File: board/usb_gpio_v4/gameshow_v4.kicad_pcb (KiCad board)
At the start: 2 copper layers, 160.8 x 51.3 mm, 27 parts, among them J1 NC3FAAH, J2 NC3FAAH, J3 NC3FAAH, J4 NC3FAAH

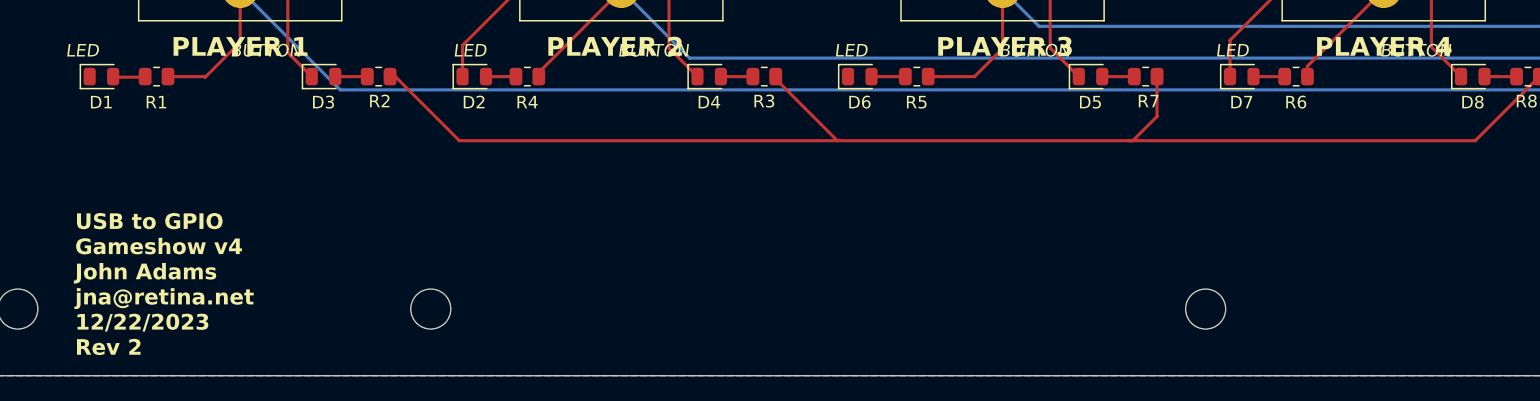
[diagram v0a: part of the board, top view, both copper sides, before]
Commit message: add test switches
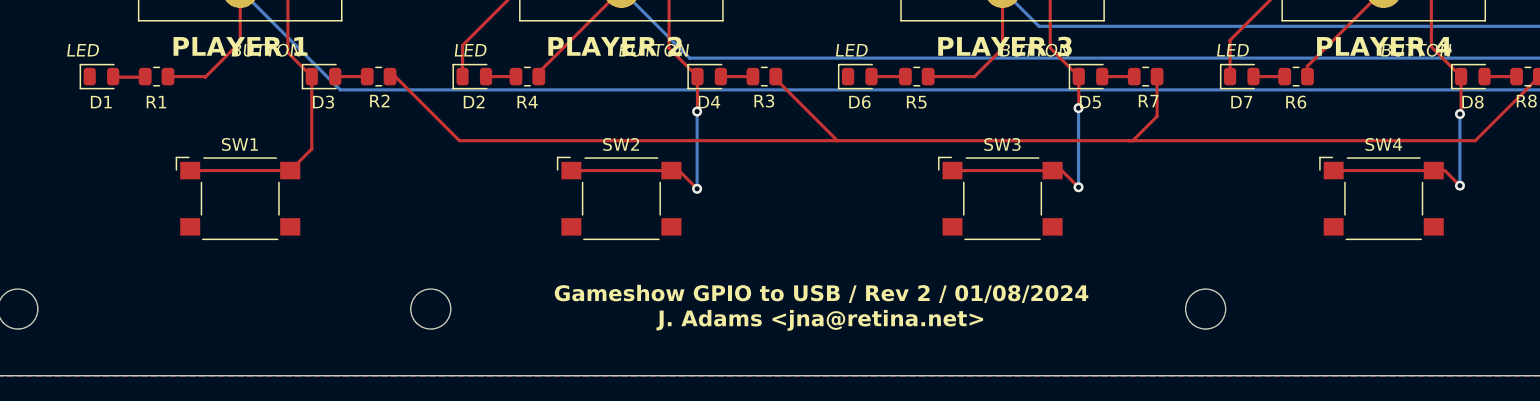
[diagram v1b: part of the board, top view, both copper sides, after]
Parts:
- added SW1: SW_SPST, Button_Switch_SMD:SW_SPST_Omron_B3FS-101xP, F.Cu at (92.7, 91.0)
- added SW2: SW_SPST, Button_Switch_SMD:SW_SPST_Omron_B3FS-101xP, F.Cu at (123.2, 91.0)
- added SW3: SW_SPST, Button_Switch_SMD:SW_SPST_Omron_B3FS-101xP, F.Cu at (153.7, 91.0)
- added SW4: SW_SPST, Button_Switch_SMD:SW_SPST_Omron_B3FS-101xP, F.Cu at (184.2, 91.0)
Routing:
- net P2_SW: track 106.9 -> 126.6 mm, vias 0 -> 2
- net P3_SW: track 75.4 -> 94.9 mm, vias 0 -> 2
- net P4_SW: track 44.3 -> 63.7 mm, vias 0 -> 2
- net P1_SW: track 122.0 -> 138.2 mm
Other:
- board text added: "Gameshow GPIO to USB / Rev 2 / 01/08/2024 J. Adams <jna@retina.net>"
- board text removed: "USB to GPIO Gameshow v4 John Adams jna@retina.net 12/22/2023 Rev 2"

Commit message: refactor code
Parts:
- moved SW4 4.52 mm to (184.2, 86.5)
- moved SW1 4.52 mm to (92.7, 86.5)
- moved SW2 4.52 mm to (123.2, 86.5)
- moved SW3 4.52 mm to (153.7, 86.5)
- moved J1 2.70 mm to (88.9, 67.2)
- moved J2 2.70 mm to (119.4, 67.2)
- moved J3 2.70 mm to (149.9, 67.2)
- moved J4 2.70 mm to (180.3, 67.2)
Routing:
- net P4_SW: track 63.7 -> 57.3 mm, vias 2 -> 0
- net GND: track 29.2 -> 35.3 mm
- net P2_LED: track 107.4 -> 112.8 mm
- net P2_SW: track 126.6 -> 121.3 mm, vias 2 -> 0
- net P3_SW: track 94.9 -> 89.8 mm, vias 2 -> 0
- net P4_LED: track 44.0 -> 47.9 mm
- net P3_LED: track 77.8 -> 81.6 mm
- net P1_LED: track 140.4 -> 144.3 mm
- net P1_SW: track 138.2 -> 135.3 mm
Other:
- board text added: "Gameshow GPIO to USB / Rev 2 / 06/13/2024 J. Adams <jna@retina.net>"
- board text removed: "Gameshow GPIO to USB / Rev 2 / 01/08/2024 J. Adams <jna@retina.net>"
